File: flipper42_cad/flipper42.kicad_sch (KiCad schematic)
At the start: 3 parts, among them IC1 EM4095, J1 1040310811, U1 ST25R3916B-AQWT

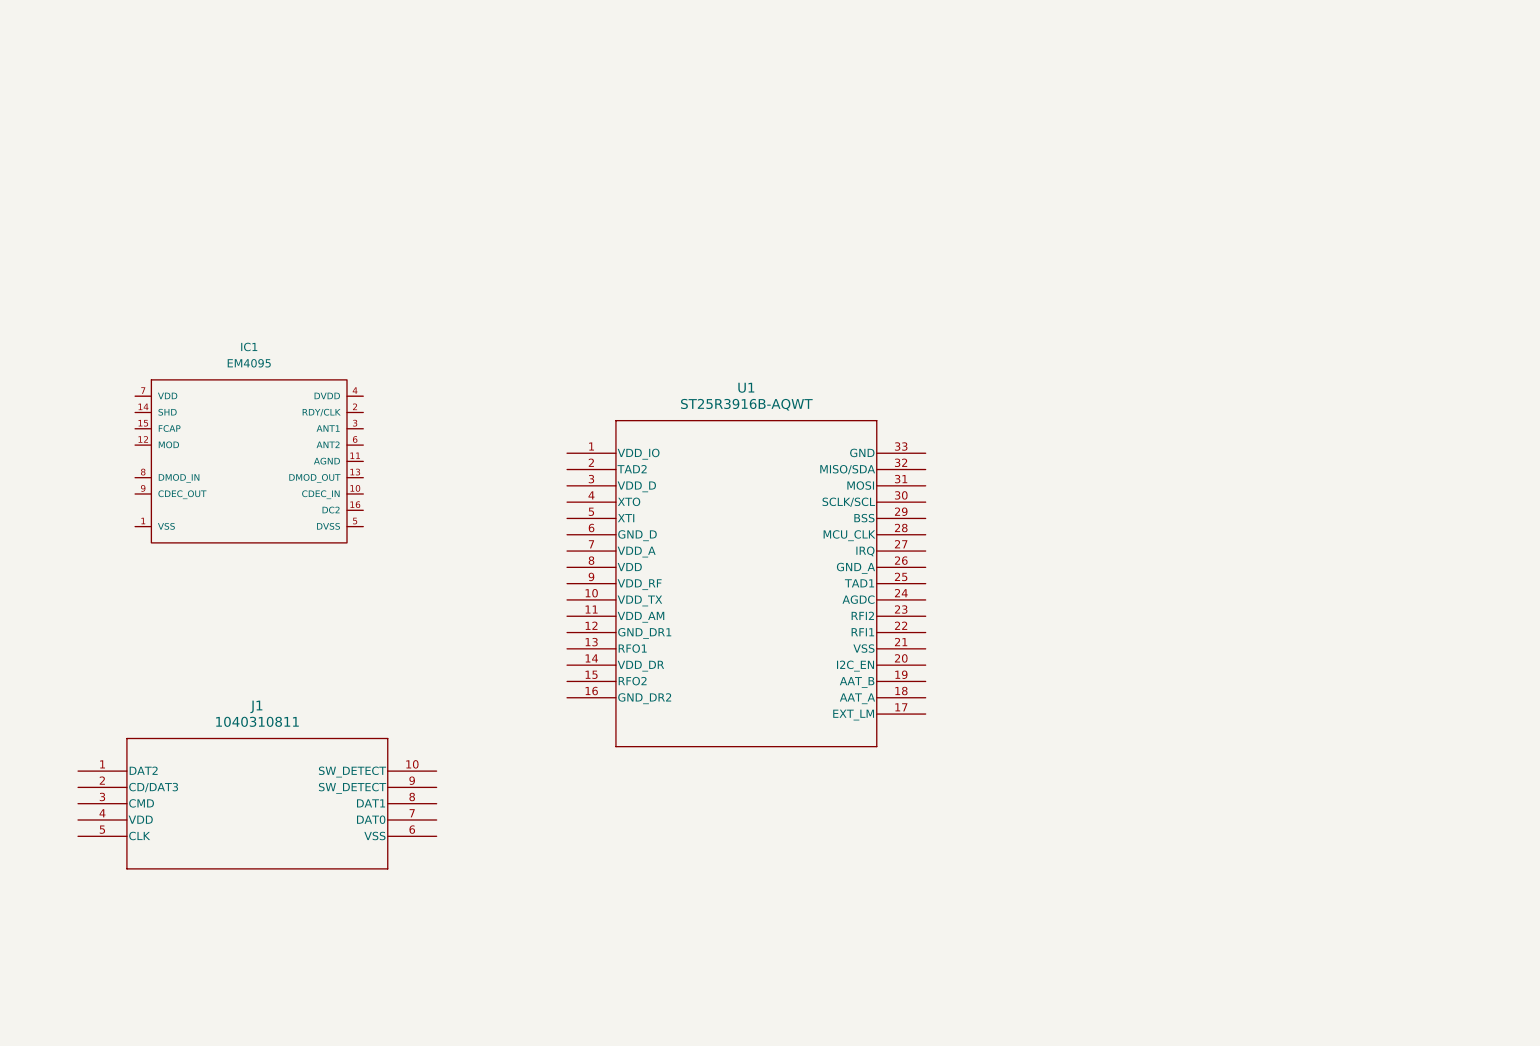
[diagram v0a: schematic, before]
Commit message: Added BOM, changed kicad and updated CDC
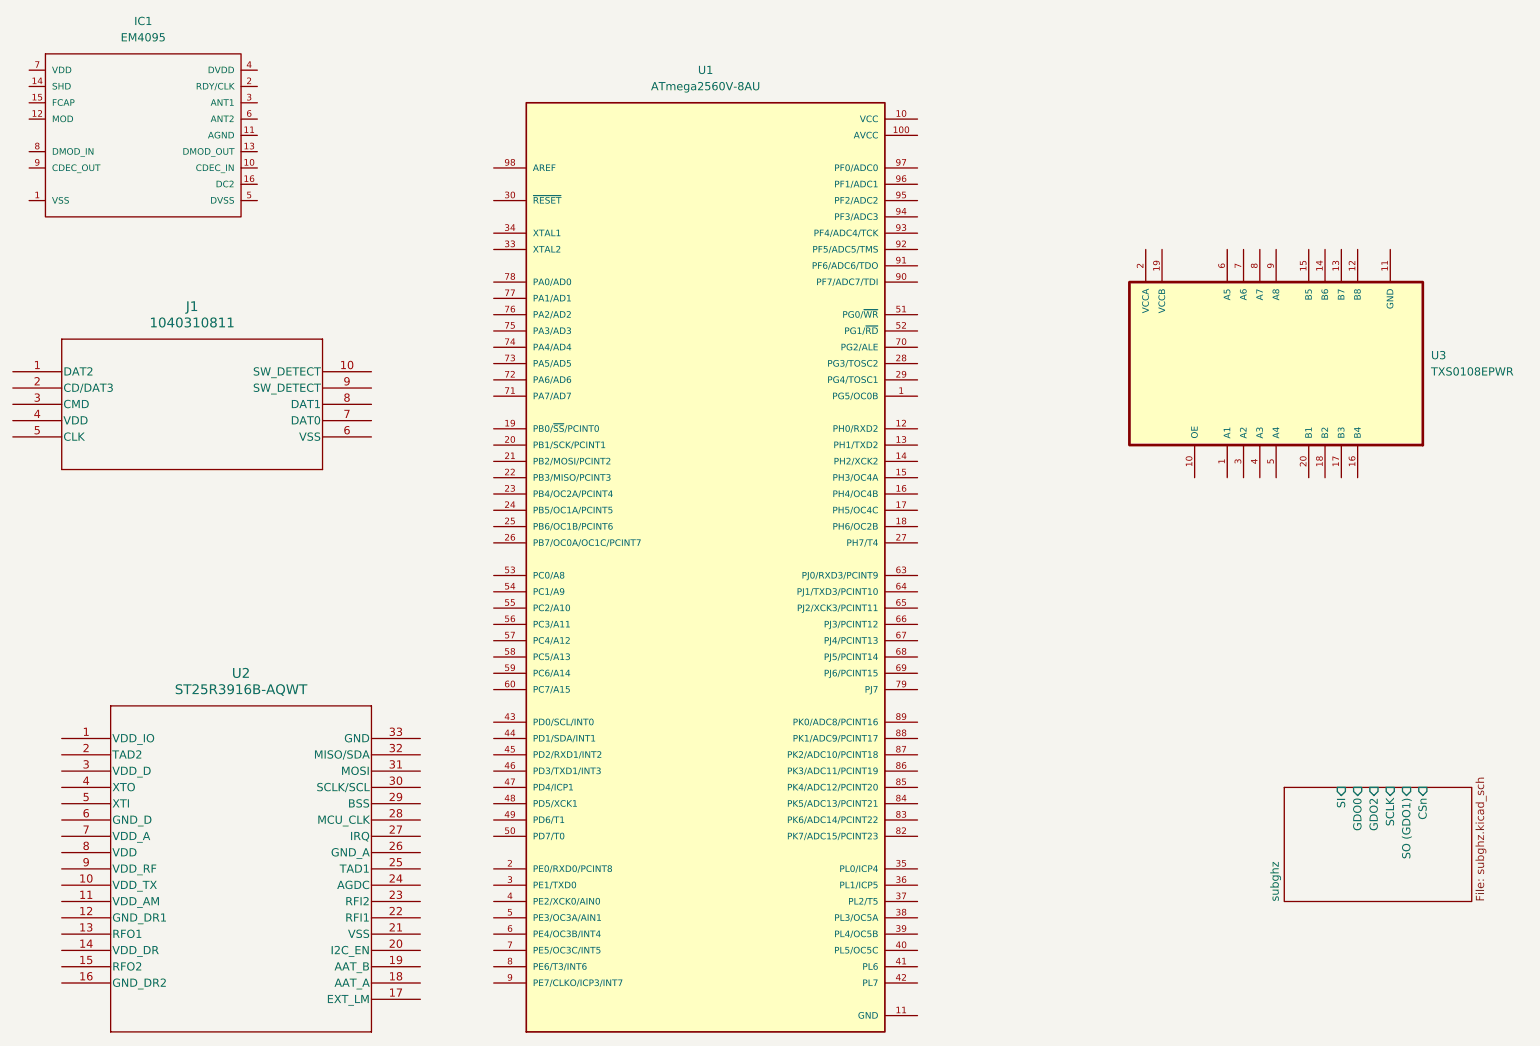
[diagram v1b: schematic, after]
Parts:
- added U1: ATmega2560V-8AU, ATmega2560V-8AU:QFP50P1600X1600X120-100N, symbol ATmega2560V-8AU:ATmega2560V-8AU
- added U3: TXS0108EPWR, TXS0108EPWR:SOP65P640X120-20N, symbol TXS0108EPWR:TXS0108EPWR
- renumbered U1 to U2
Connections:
- new net GND: U1.11 (GND), U1.32 (GND), U1.62 (GND), U1.81 (GND), U1.99 (GND)
- new net VCC: U1.10 (VCC), U1.31 (VCC), U1.61 (VCC), U1.80 (VCC)
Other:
- added sheet subghz (subghz.kicad_sch)
- moved on the sheet: IC1, J1, U2
